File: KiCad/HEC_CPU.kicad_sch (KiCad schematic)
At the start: 11 parts, among them J3 Conn_02x05_Odd_Even, U1 Z80CPU, U16 74LS32, U18 74LS138, U20 74LS574, U21 74LS574, U22 74LS02, U23 74LS74, U34 74LS393, U7 28C256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

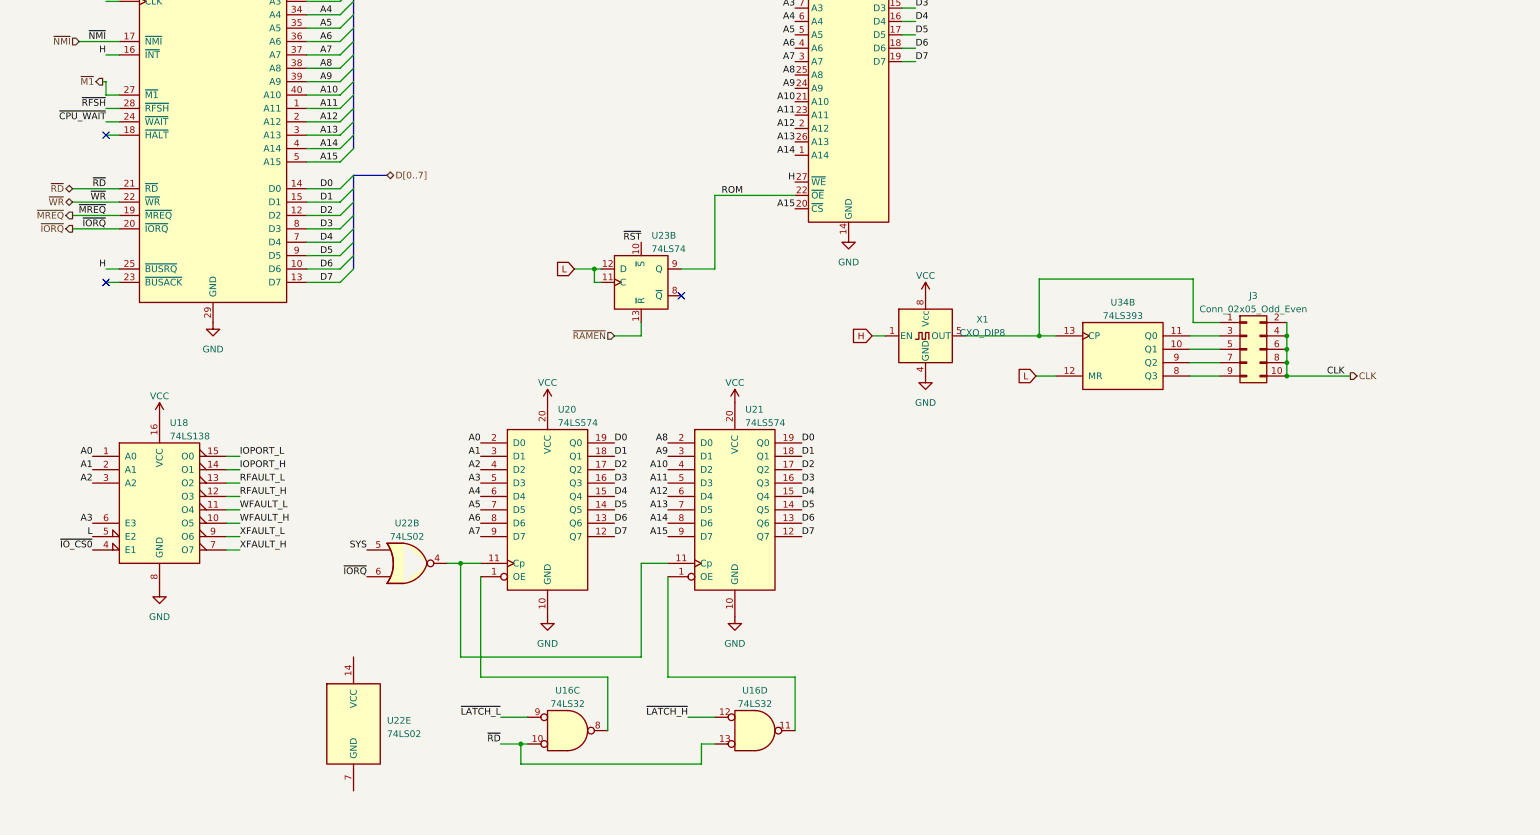
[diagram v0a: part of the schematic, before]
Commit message: PCB Update
Some part placement, some routing, some change in schematic for easier PCB routing.
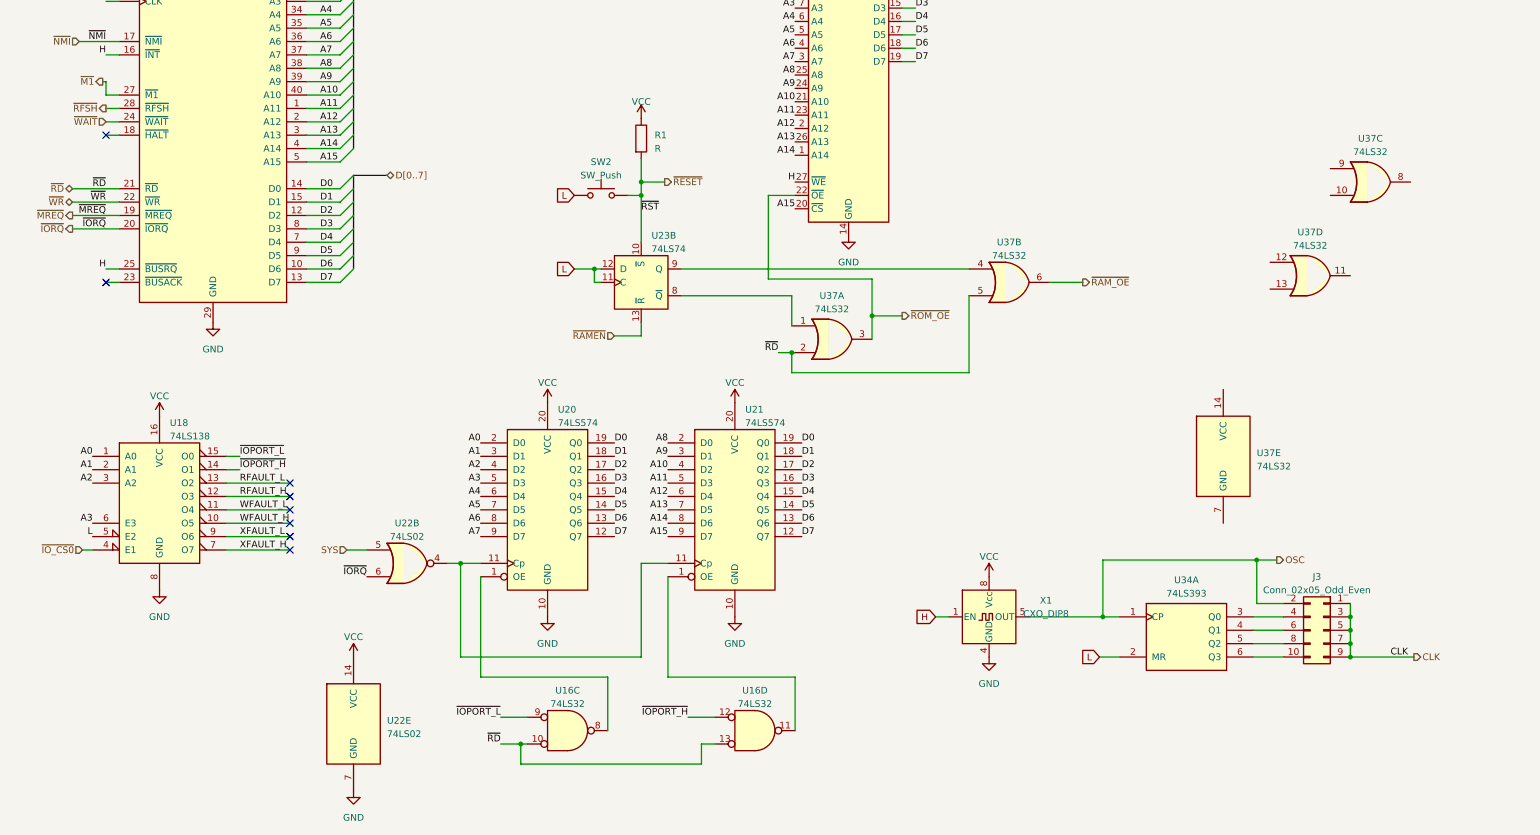
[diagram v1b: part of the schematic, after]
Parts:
- removed U34: 74LS393, Package_DIP:DIP-14_W7.62mm_Socket, symbol 74xx:74LS393
- added R1: R, Resistor_THT:R_Axial_DIN0207_L6.3mm_D2.5mm_P7.62mm_Horizontal, symbol Device:R
- added SW2: SW_Push, Button_Switch_THT:SW_PUSH_6mm, symbol Switch:SW_Push
- added U34: 74LS393, Package_DIP:DIP-14_W7.62mm_Socket, symbol 74xx:74LS393
- added U37: 74LS32, symbol 74xx:74LS32
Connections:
- net ~{LATCH_H} is gone; now on net ~{IOPORT_H}: U16.12
- net ~{LATCH_L} is gone; now on net ~{IOPORT_L}: U16.9
- net CLK: now also J3.1 (Pin_1), J3.3 (Pin_3), J3.5 (Pin_5), J3.7 (Pin_7), J3.9 (Pin_9); no longer J3.10 (Pin_10), J3.2 (Pin_2), J3.4 (Pin_4), J3.6 (Pin_6), J3.8 (Pin_8)
- net GND: now also U22.7 (GND)
- net L: now also SW2.2, U34.2 (MR)
- net VCC: now also U22.14 (VCC), R1.1
- net ~{RD}: now also U37.2, U37.5
- net OSC: now reaches X1.5 (OUT)
- net OSC: now also J3.2 (Pin_2), U34.1 (CP); no longer J3.1 (Pin_1)
- net at U23.8 (~{Q}): now also U37.1
- net IOPORT_H renamed ~{IOPORT_H}
- net IOPORT_L renamed ~{IOPORT_L}
- net ROM: no longer names the net of U23.9 (Q)
- net ROM: now also U37.4; no longer U7.22 (~{OE})
- net ~{CPU_WAIT} renamed ~{WAIT}
- net ~{RST} renamed ~{RESET}
- net ~{RESET}: now also R1.2, SW2.1
- new net: J3.4 (Pin_4), U34.3 (Q0)
- new net: J3.6 (Pin_6), U34.4 (Q1)
- new net: J3.8 (Pin_8), U34.5 (Q2)
- new net: J3.10 (Pin_10), U34.6 (Q3)
- new net ~{RAM_OE}: U37.6
- new net ~{ROM_OE}: U37.3, U7.22 (~{OE})
- no-connect marks 3 -> 8
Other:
- moved on the sheet: J3, X1

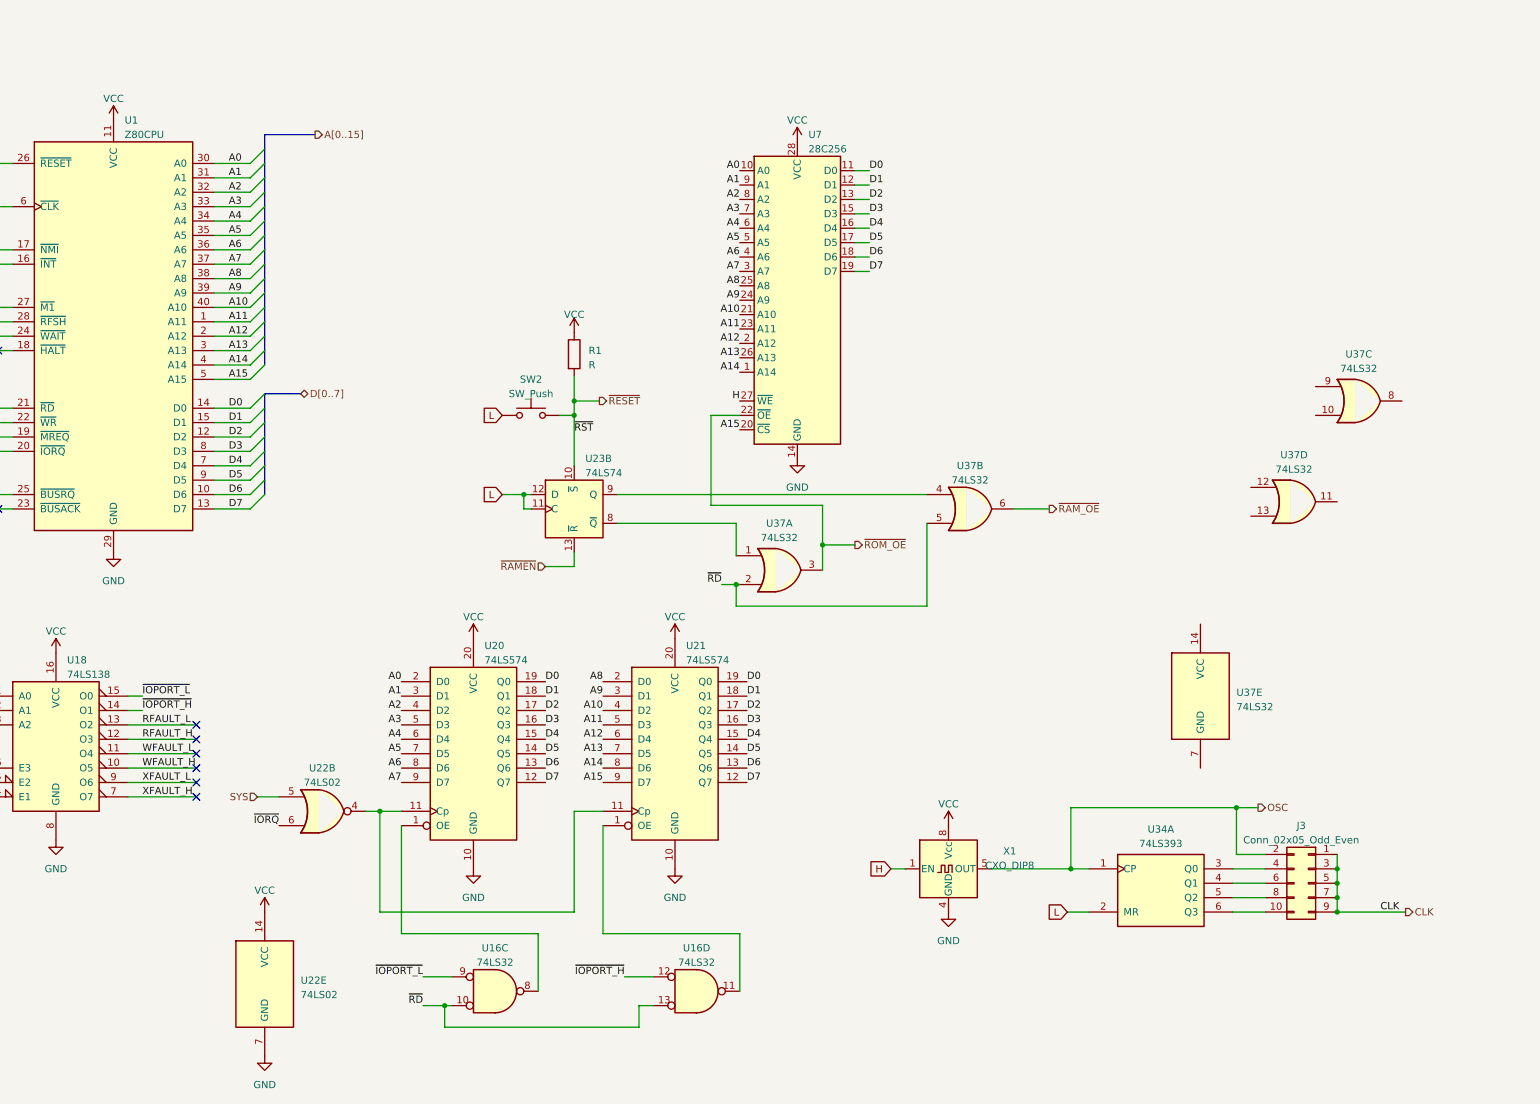
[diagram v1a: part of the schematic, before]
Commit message: Add POST code circuit
Add circuit to show POST code using I register on Z80 to assist debugging.
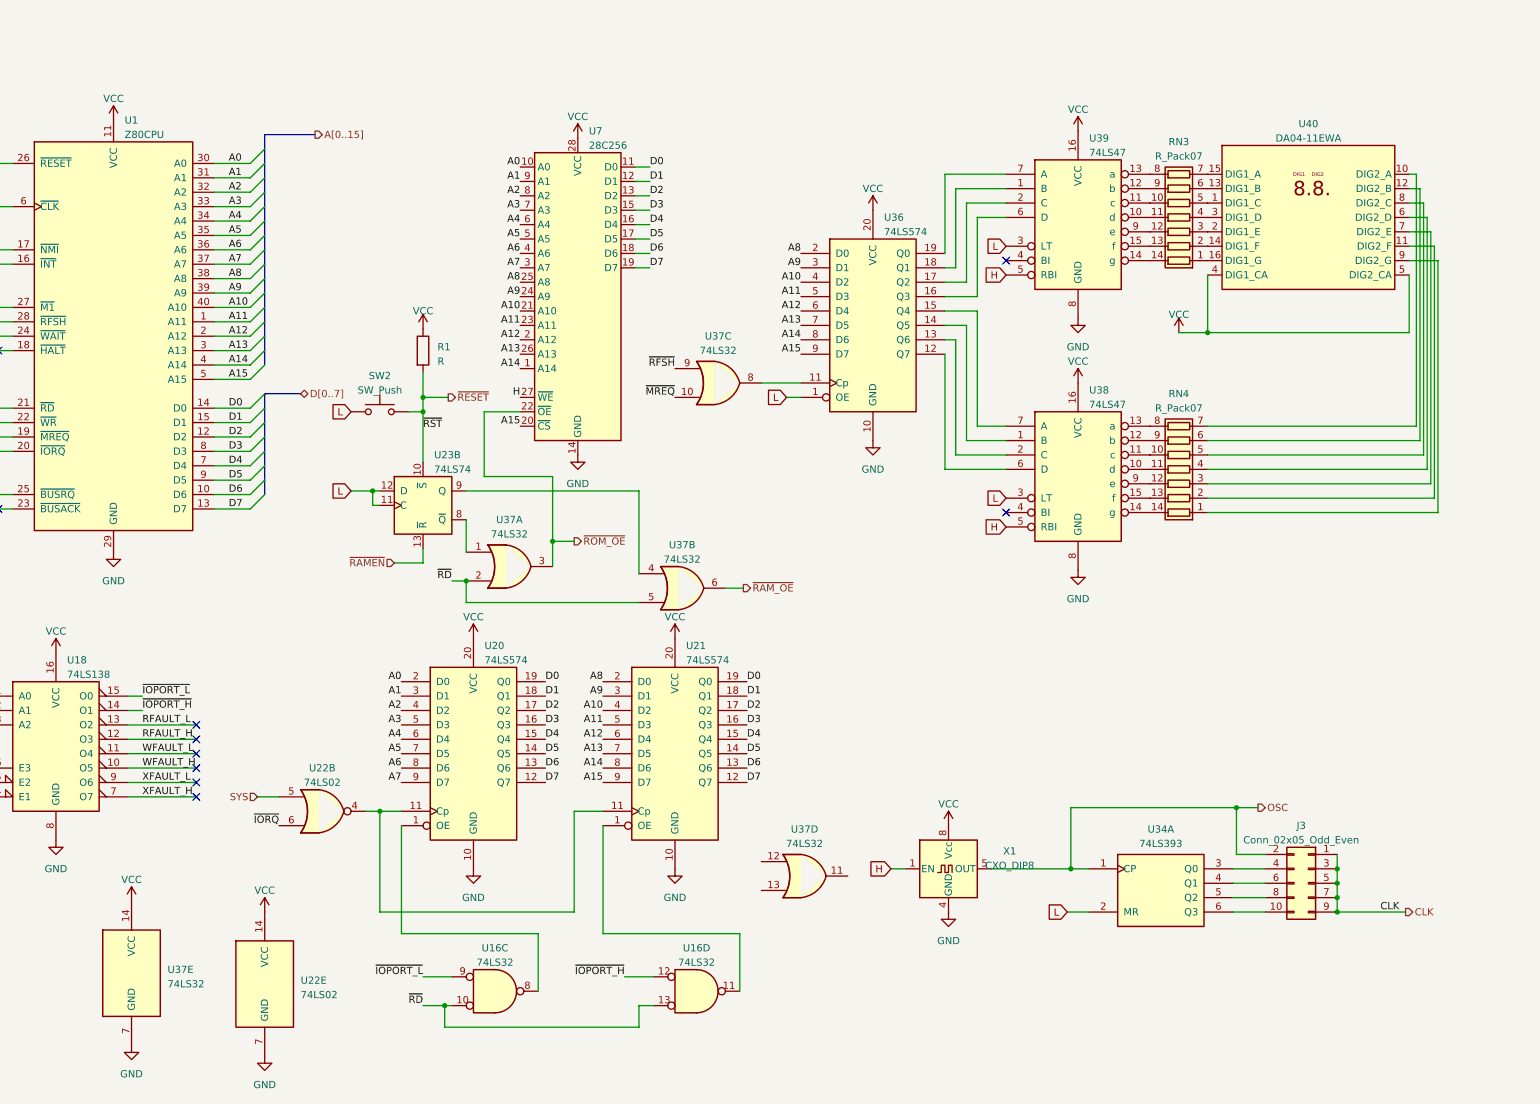
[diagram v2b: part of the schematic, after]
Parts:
- added RN3, RN4: R_Pack07, Package_DIP:DIP-14_W7.62mm, symbol Device:R_Pack07
- added U36: 74LS574, Package_DIP:DIP-20_W7.62mm_Socket, symbol 74xx:74LS574
- added U38, U39: 74LS47, Package_DIP:DIP-16_W7.62mm_Socket, symbol 74xx:74LS47
- added U40: DA04-11EWA, Display_7Segment:DA04-11SURKWA, symbol Display_Character:DA04-11EWA
- U37: footprint (none) -> Package_DIP:DIP-14_W7.62mm_Socket
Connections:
- net A10: now also U36.4 (D2)
- net A11: now also U36.5 (D3)
- net A12: now also U36.6 (D4)
- net A13: now also U36.7 (D5)
- net A14: now also U36.8 (D6)
- net A15: now also U36.9 (D7)
- net A8: now also U36.2 (D0)
- net A9: now also U36.3 (D1)
- net GND: now also U37.7 (GND), U36.10 (GND), U38.8 (GND), U39.8 (GND)
- net H: now also U38.5 (RBI), U39.5 (RBI)
- net L: now also U36.1 (OE), U38.3 (LT), U39.3 (LT)
- net VCC: now also U37.14 (VCC), U36.20 (VCC), U38.16 (VCC), U39.16 (VCC), U40.4 (DIG1_CA), U40.5 (DIG2_CA)
- net ~{MREQ}: now also U37.10
- net ~{RFSH}: now also U37.9
- net at U37.8: now also U36.11 (Cp)
- new net: RN4.1 (R1.1), U40.9 (DIG2_G)
- new net: RN4.10 (R5.2), U38.11 (c)
- new net: RN4.11 (R4.2), U38.10 (d)
- new net: RN4.12 (R3.2), U38.9 (e)
- new net: RN4.13 (R2.2), U38.15 (f)
- new net: RN4.14 (R1.2), U38.14 (g)
- new net: RN4.2 (R2.1), U40.11 (DIG2_F)
- new net: RN4.3 (R3.1), U40.7 (DIG2_E)
- new net: RN4.4 (R4.1), U40.6 (DIG2_D)
- new net: RN4.5 (R5.1), U40.8 (DIG2_C)
- new net: RN4.6 (R6.1), U40.12 (DIG2_B)
- new net: RN4.7 (R7.1), U40.10 (DIG2_A)
- new net: RN4.8 (R7.2), U38.13 (a)
- new net: RN4.9 (R6.2), U38.12 (b)
- new net: U36.14 (Q5), U38.1 (B)
- new net: U36.13 (Q6), U38.2 (C)
- new net: U36.12 (Q7), U38.6 (D)
- new net: U36.15 (Q4), U38.7 (A)
- new net: RN3.5 (R5.1), U40.1 (DIG1_C)
- new net: RN3.6 (R6.1), U40.13 (DIG1_B)
- new net: RN3.2 (R2.1), U40.14 (DIG1_F)
- new net: RN3.7 (R7.1), U40.15 (DIG1_A)
- new net: RN3.1 (R1.1), U40.16 (DIG1_G)
- new net: RN3.3 (R3.1), U40.2 (DIG1_E)
- new net: RN3.4 (R4.1), U40.3 (DIG1_D)
- new net: U36.16 (Q3), U39.6 (D)
- new net: U36.17 (Q2), U39.2 (C)
- new net: U36.18 (Q1), U39.1 (B)
- new net: U36.19 (Q0), U39.7 (A)
- new net: RN3.10 (R5.2), U39.11 (c)
- new net: RN3.11 (R4.2), U39.10 (d)
- new net: RN3.12 (R3.2), U39.9 (e)
- new net: RN3.13 (R2.2), U39.15 (f)
- new net: RN3.14 (R1.2), U39.14 (g)
- new net: RN3.8 (R7.2), U39.13 (a)
- new net: RN3.9 (R6.2), U39.12 (b)
- no-connect marks 8 -> 10
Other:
- moved on the sheet: R1, SW2, U23B, U37A, U37B, U37C, U37D, U37E, U7
